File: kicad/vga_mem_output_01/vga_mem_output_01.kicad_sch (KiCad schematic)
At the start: 18 parts, among them J1 Conn_01x03_Socket, J2 Conn_01x02_Socket, J3 Conn_01x08_Socket, U1 74LS08, U2 74LS08

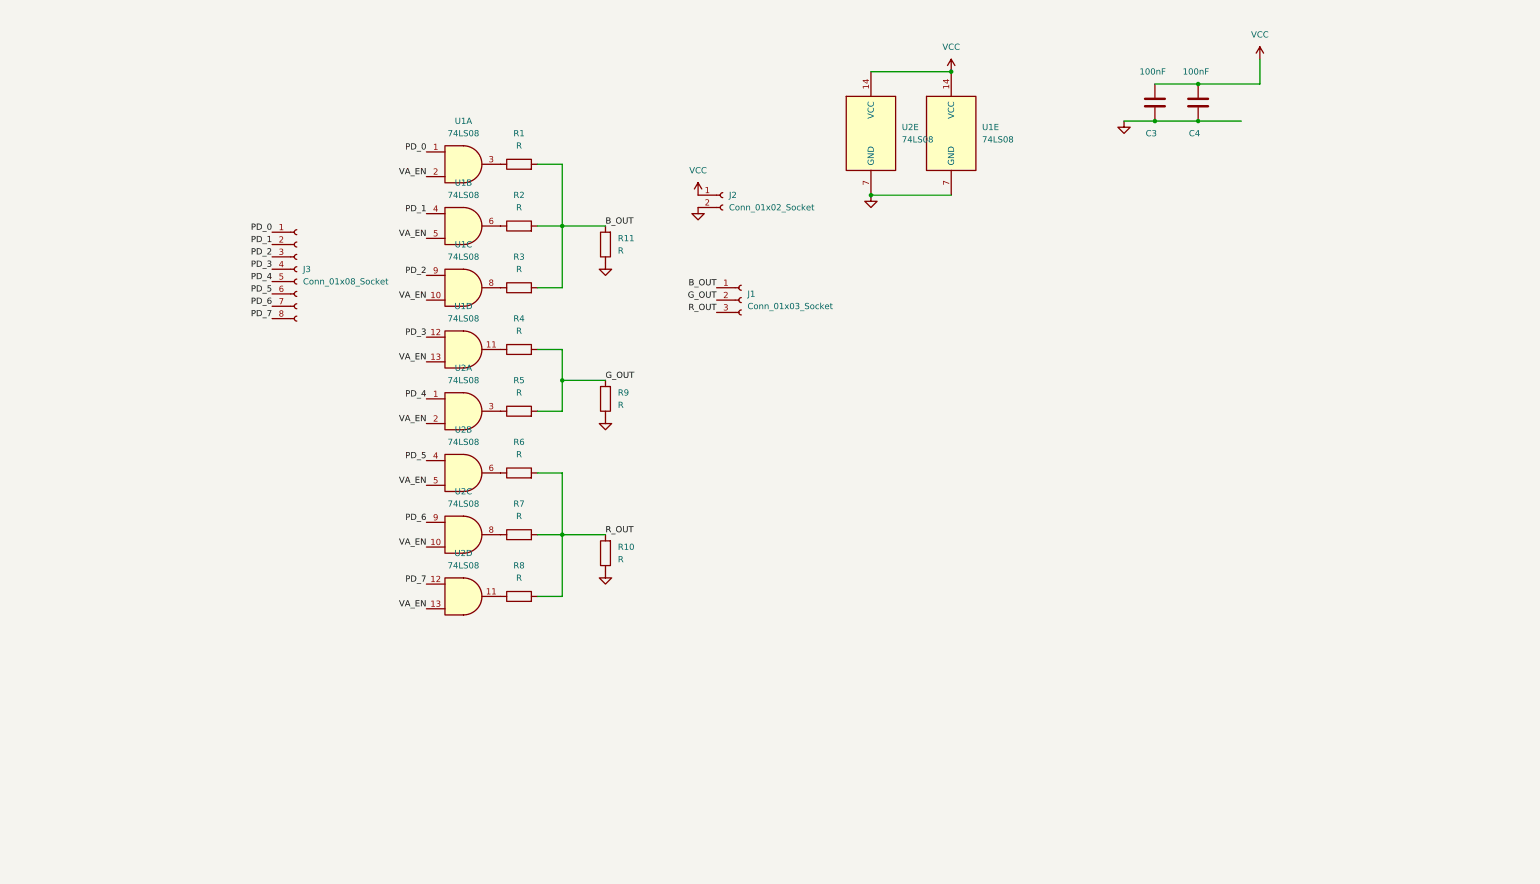
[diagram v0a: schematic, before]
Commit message: more routing on 2 layer version (abandon for 4 layer version)
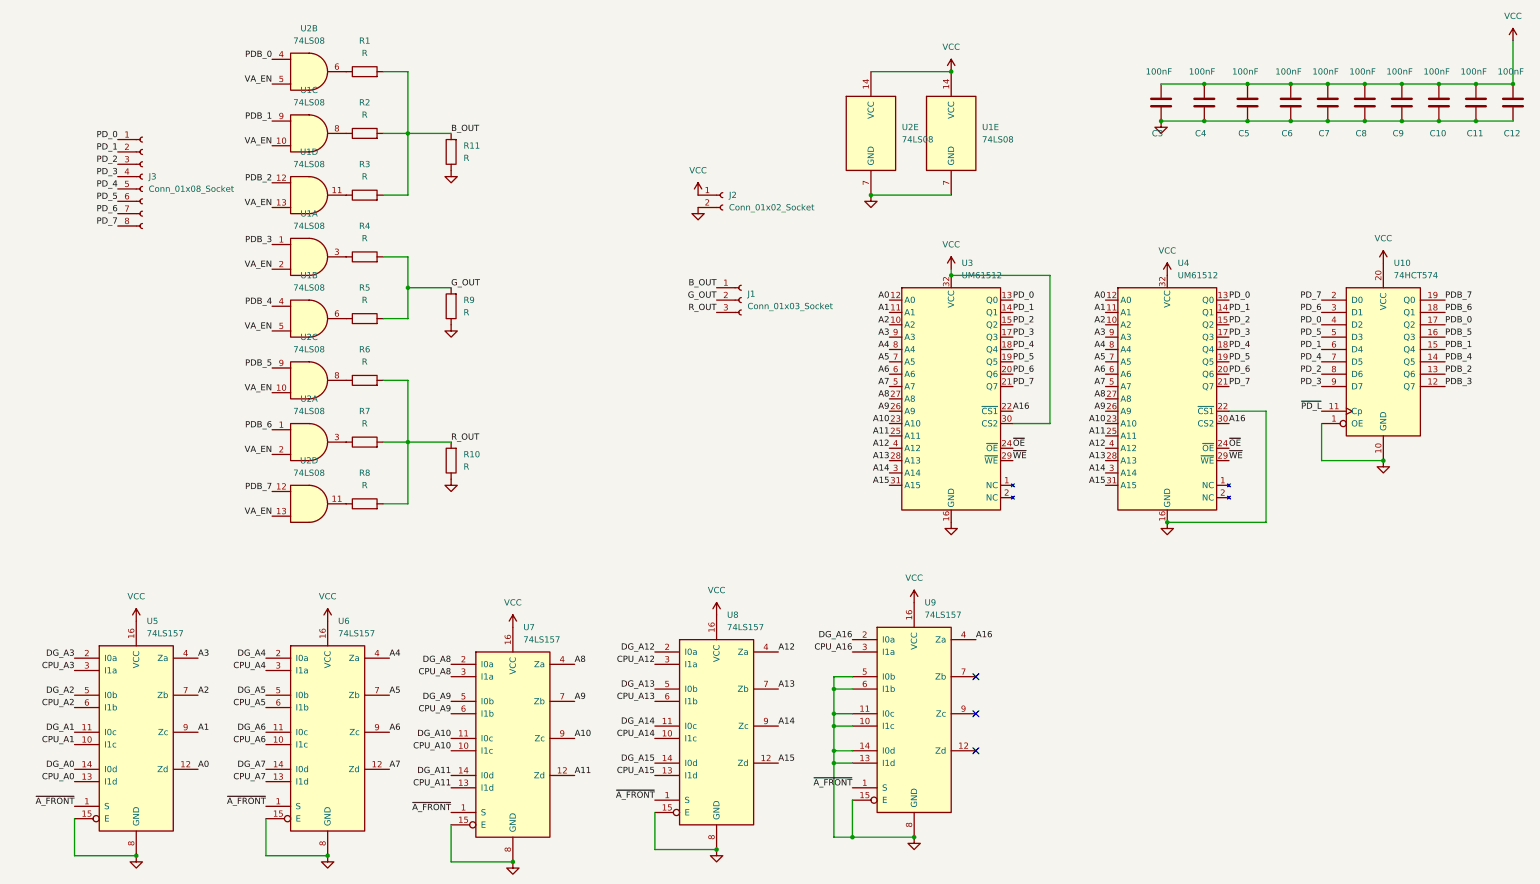
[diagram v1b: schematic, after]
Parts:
- added C10, C11, C12, C5, C6, C7, C8, C9: 100nF, Capacitor_SMD:C_0805_2012Metric_Pad1.18x1.45mm_HandSolder, symbol Device:C
- added U10: 74HCT574, Package_SO:SO-20_5.3x12.6mm_P1.27mm, symbol 74xx:74HCT574
- added U3, U4: UM61512, Package_DIP:DIP-32_W7.62mm, symbol mem:UM61512
- added U5, U6, U7, U8, U9: 74LS157, Package_SO:SO-16_3.9x9.9mm_P1.27mm, symbol 74xx:74LS157
- R1, R10, R11, R2, R3, R4, R5, R6, R7, R8, R9: footprint Resistor_THT:R_Axial_DIN0207_L6.3mm_D2.5mm_P10.16mm_Horizontal -> Resistor_THT:R_Axial_DIN0204_L3.6mm_D1.6mm_P7.62mm_Horizontal
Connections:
- net GND: now also C10.2, C11.2, C12.2, C5.2, C6.2, C7.2, C8.2, C9.2, U10.1 (OE), U10.10 (GND), U3.16 (GND), U4.16 (GND), U4.22 (~{CS1}), U5.15 (E), U5.8 (GND), U6.15 (E), U6.8 (GND), U7.15 (E), U7.8 (GND), U8.15 (E), U8.8 (GND), U9.10 (I1c), U9.11 (I0c), U9.13 (I1d), U9.14 (I0d), U9.15 (E), U9.5 (I0b), U9.6 (I1b), U9.8 (GND)
- net PD_0: now also U10.4 (D2), U3.13 (Q0), U4.13 (Q0); no longer U1.1
- net PD_1: now also U10.6 (D4), U3.14 (Q1), U4.14 (Q1); no longer U1.4
- net PD_2: now also U10.8 (D6), U3.15 (Q2), U4.15 (Q2); no longer U1.9
- net PD_3: now also U10.9 (D7), U3.17 (Q3), U4.17 (Q3); no longer U1.12
- net PD_4: now also U10.7 (D5), U3.18 (Q4), U4.18 (Q4); no longer U2.1
- net PD_5: now also U10.5 (D3), U3.19 (Q5), U4.19 (Q5); no longer U2.4
- net PD_6: now also U10.3 (D1), U3.20 (Q6), U4.20 (Q6); no longer U2.9
- net PD_7: now also U10.2 (D0), U3.21 (Q7), U4.21 (Q7); no longer U2.12
- net VCC: now also C10.1, C11.1, C12.1, C5.1, C6.1, C7.1, C8.1, C9.1, U10.20 (VCC), U3.30 (CS2), U3.32 (VCC), U4.32 (VCC), U5.16 (VCC), U6.16 (VCC), U7.16 (VCC), U8.16 (VCC), U9.16 (VCC)
- net at R6.1: now also U2.8; no longer U2.6
- net at R5.1: now also U1.6; no longer U2.3
- net at R1.1: now also U2.6; no longer U1.3
- net at R2.1: now also U1.8; no longer U1.6
- net at R4.1: now also U1.3; no longer U1.11
- net at R3.1: now also U1.11; no longer U1.8
- net at R7.1: now also U2.3; no longer U2.8
- new net A0: U3.12 (A0), U4.12 (A0), U5.12 (Zd)
- new net A1: U3.11 (A1), U4.11 (A1), U5.9 (Zc)
- new net A10: U3.23 (A10), U4.23 (A10), U7.9 (Zc)
- new net A11: U3.25 (A11), U4.25 (A11), U7.12 (Zd)
- new net A12: U3.4 (A12), U4.4 (A12), U8.4 (Za)
- new net A13: U3.28 (A13), U4.28 (A13), U8.7 (Zb)
- new net A14: U3.3 (A14), U4.3 (A14), U8.9 (Zc)
- new net A15: U3.31 (A15), U4.31 (A15), U8.12 (Zd)
- new net A16: U3.22 (~{CS1}), U4.30 (CS2), U9.4 (Za)
- new net A2: U3.10 (A2), U4.10 (A2), U5.7 (Zb)
- new net A3: U3.9 (A3), U4.9 (A3), U5.4 (Za)
- new net A4: U3.8 (A4), U4.8 (A4), U6.4 (Za)
- new net A5: U3.7 (A5), U4.7 (A5), U6.7 (Zb)
- new net A6: U3.6 (A6), U4.6 (A6), U6.9 (Zc)
- new net A7: U3.5 (A7), U4.5 (A7), U6.12 (Zd)
- new net A8: U3.27 (A8), U4.27 (A8), U7.4 (Za)
- new net A9: U3.26 (A9), U4.26 (A9), U7.7 (Zb)
- new net CPU_A0: U5.13 (I1d)
- new net CPU_A1: U5.10 (I1c)
- new net CPU_A10: U7.10 (I1c)
- new net CPU_A11: U7.13 (I1d)
- new net CPU_A12: U8.3 (I1a)
- new net CPU_A13: U8.6 (I1b)
- new net CPU_A14: U8.10 (I1c)
- new net CPU_A15: U8.13 (I1d)
- new net CPU_A16: U9.3 (I1a)
- new net CPU_A2: U5.6 (I1b)
- new net CPU_A3: U5.3 (I1a)
- new net CPU_A4: U6.3 (I1a)
- new net CPU_A5: U6.6 (I1b)
- new net CPU_A6: U6.10 (I1c)
- new net CPU_A7: U6.13 (I1d)
- new net CPU_A8: U7.3 (I1a)
- new net CPU_A9: U7.6 (I1b)
- new net DG_A0: U5.14 (I0d)
- new net DG_A1: U5.11 (I0c)
- new net DG_A10: U7.11 (I0c)
- new net DG_A11: U7.14 (I0d)
- new net DG_A12: U8.2 (I0a)
- new net DG_A13: U8.5 (I0b)
- new net DG_A14: U8.11 (I0c)
- new net DG_A15: U8.14 (I0d)
- new net DG_A16: U9.2 (I0a)
- new net DG_A2: U5.5 (I0b)
- new net DG_A3: U5.2 (I0a)
- new net DG_A4: U6.2 (I0a)
- new net DG_A5: U6.5 (I0b)
- new net DG_A6: U6.11 (I0c)
- new net DG_A7: U6.14 (I0d)
- new net DG_A8: U7.2 (I0a)
- new net DG_A9: U7.5 (I0b)
- new net PDB_0: U10.17 (Q2), U2.4
- new net PDB_1: U1.9, U10.15 (Q4)
- new net PDB_2: U1.12, U10.13 (Q6)
- new net PDB_3: U1.1, U10.12 (Q7)
- new net PDB_4: U1.4, U10.14 (Q5)
- new net PDB_5: U10.16 (Q3), U2.9
- new net PDB_6: U10.18 (Q1), U2.1
- new net PDB_7: U10.19 (Q0), U2.12
- new net ~{A_FRONT}: U5.1 (S), U6.1 (S), U7.1 (S), U8.1 (S), U9.1 (S)
- new net ~{OE}: U3.24 (~{OE}), U4.24 (~{OE})
- new net ~{PD_L}: U10.11 (Cp)
- new net ~{WE}: U3.29 (~{WE}), U4.29 (~{WE})
- no-connect marks 0 -> 3
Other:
- moved on the sheet: C3, C4, J3, R1, R10, R11, R2, R3, R4, R5, R6, R7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
